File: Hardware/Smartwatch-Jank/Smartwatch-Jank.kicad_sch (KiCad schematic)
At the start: 11 parts, among them J1 Conn_01x20, U1 2472

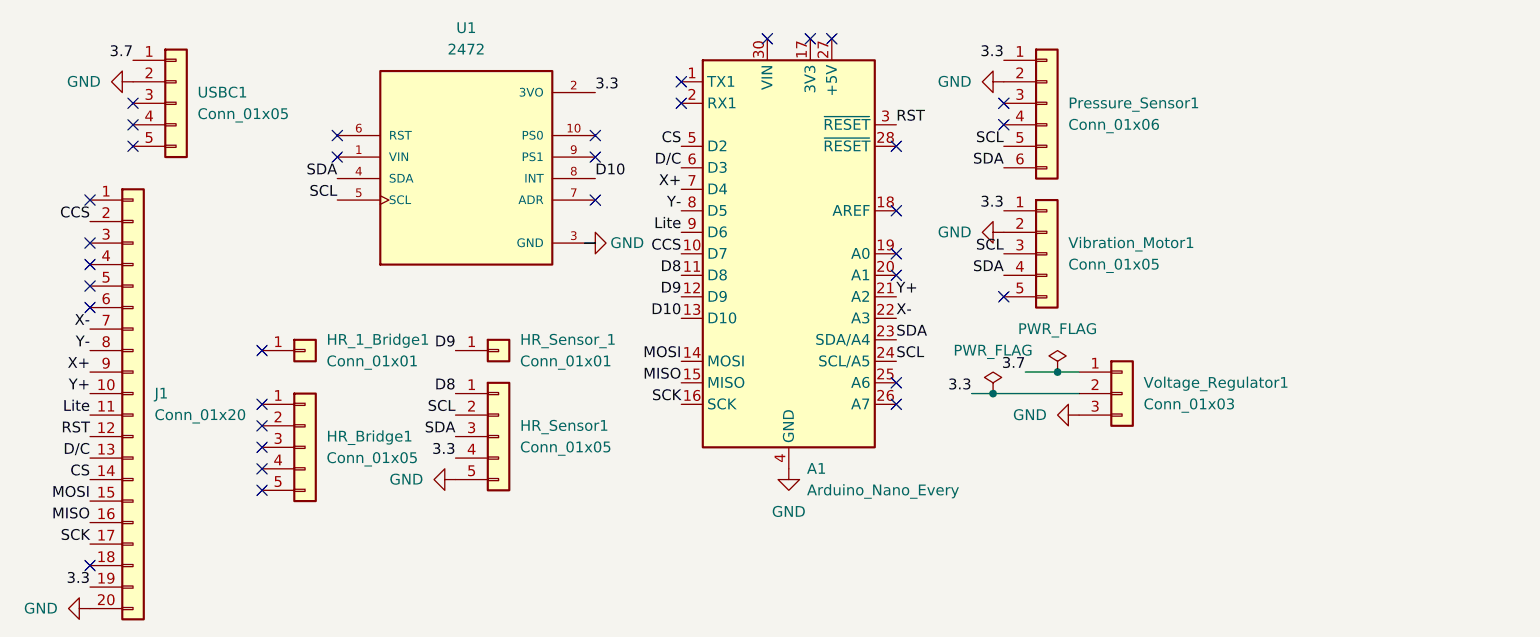
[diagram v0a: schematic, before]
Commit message: Replaced BNO055 to ICM20248 for more accurate IMU tracking
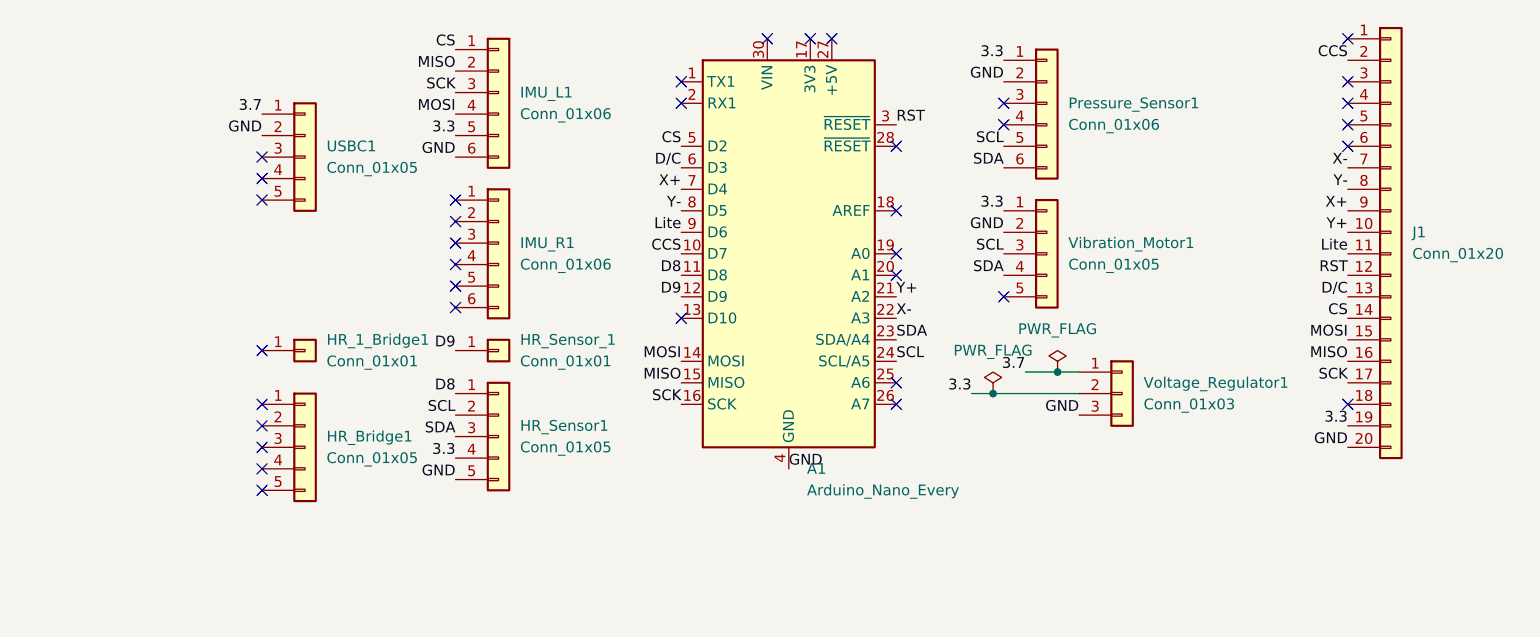
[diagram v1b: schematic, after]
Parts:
- removed U1: 2472, BNO055:BNO055, symbol BNO055:2472
- added IMU_L1, IMU_R1: Conn_01x06, Connector_PinHeader_2.54mm:PinHeader_1x06_P2.54mm_Vertical, symbol Connector_Generic:Conn_01x06
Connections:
- net 3.3: now also IMU_L1.5 (Pin_5)
- net CS: now also IMU_L1.1 (Pin_1)
- net GND: now also IMU_L1.6 (Pin_6)
- net MISO: now also IMU_L1.2 (Pin_2)
- net MOSI: now also IMU_L1.4 (Pin_4)
- net SCK: now also IMU_L1.3 (Pin_3)
- net D10: no longer names the net of A1.13 (D10)
- no-connect marks 34 -> 36
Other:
- moved on the sheet: J1, USBC1
